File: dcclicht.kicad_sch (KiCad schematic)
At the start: 46 parts, among them J101 Power IN, J102 Debug, J103 CAN, Q101 BC860, SW101 Term, SW102 Reset, SW103 User, U101 AMS1117-3.3, U102 EL817S1(C)(TU)-F, U103 EL817S1(C)(TU)-F, U104 STM32F103CBTx, U105 TJA1042T, U106 ATECC608B-MAVDA-S, Y101 8MHz, Y102 32k

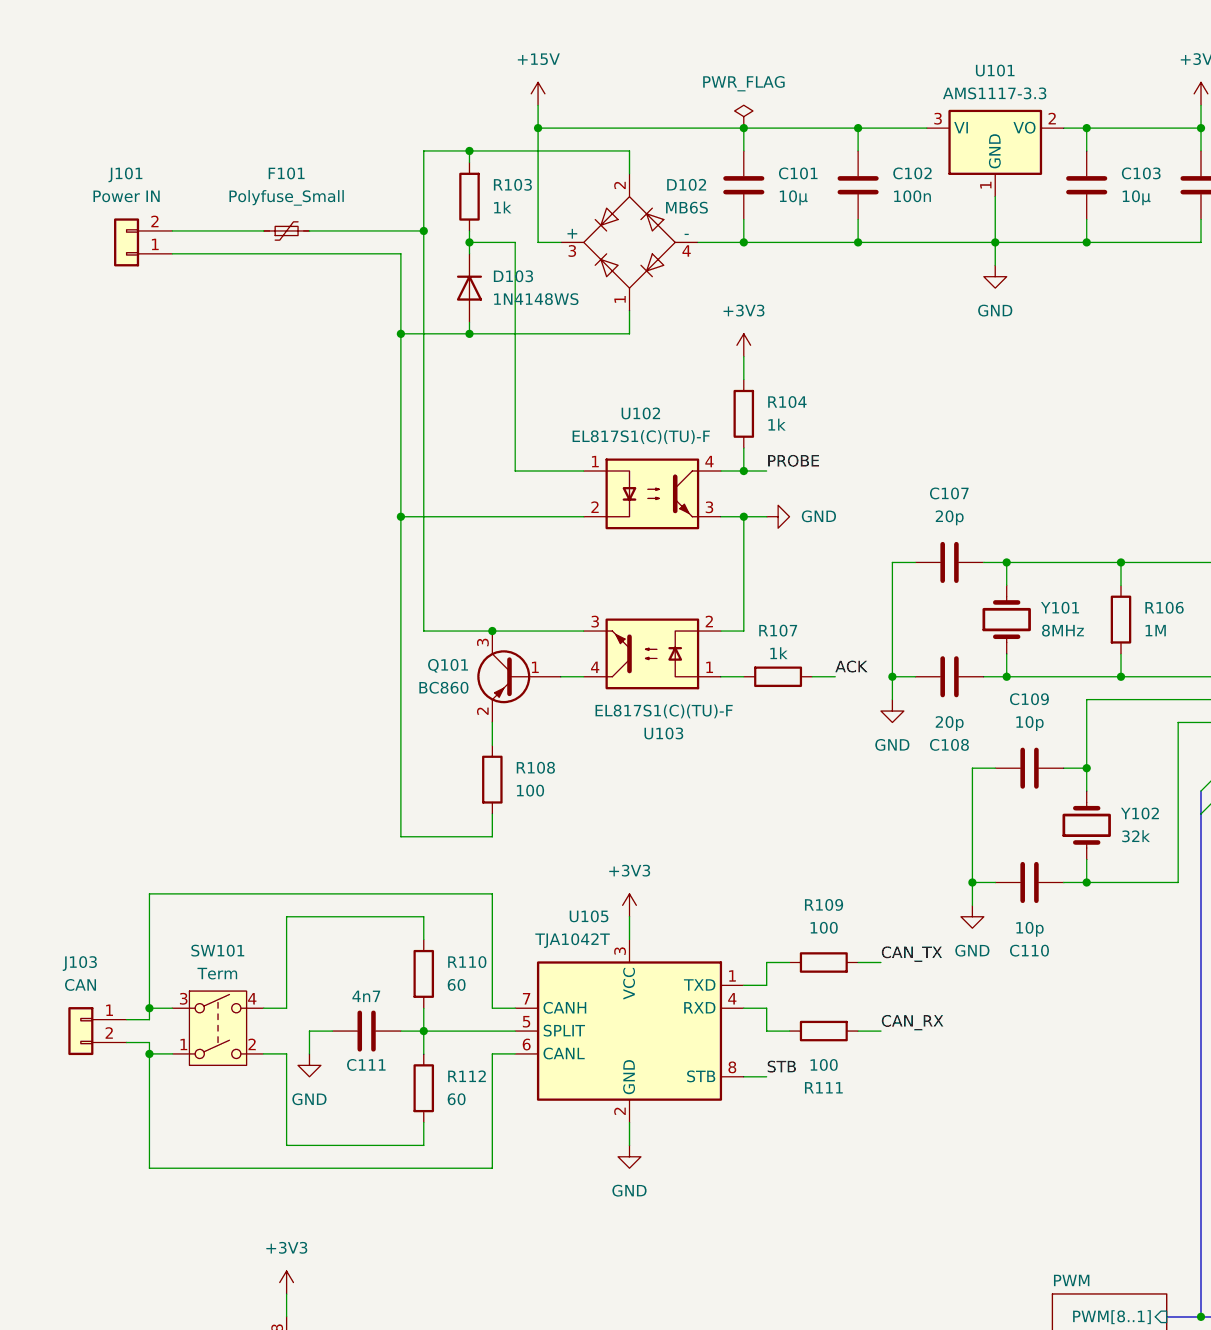
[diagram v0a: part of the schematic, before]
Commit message: Rework parts and order informations
Signed-off-by: Benedikt Spranger <b.spranger@linutronix.de>
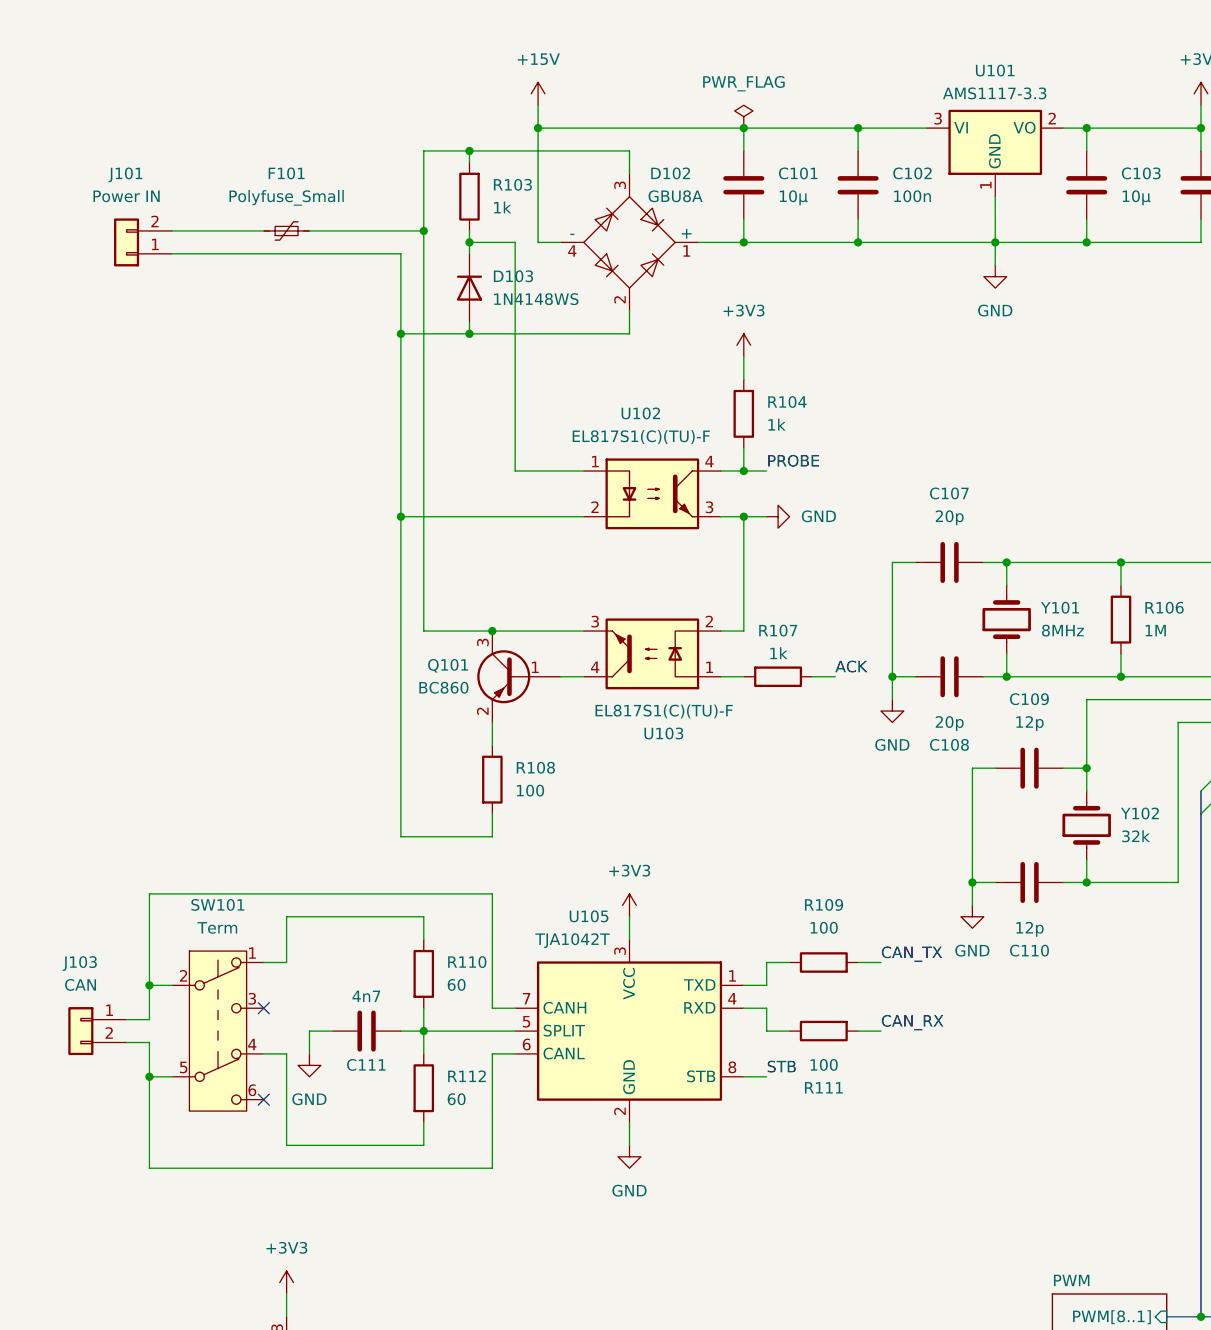
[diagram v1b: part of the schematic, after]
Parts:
- removed D102: MB6S, Package_TO_SOT_SMD:TO-269AA, symbol Diode_Bridge:MB6S
- removed SW101: Term, symbol Switch:SW_DPST
- added D102: GBU8A, Diode_THT:Diode_Bridge_Vishay_GBU, symbol Diode_Bridge:GBU8A
- added SW101: Term, Button_Switch_THT:SW_Push_2P2T_Toggle_CK_PVA2xxH1xxxxxxV2, symbol Switch:SW_Push_DPDT
- C101, C103: footprint (none) -> Capacitor_SMD:C_1206_3216Metric; LCSC# (none) -> C13585; Manufacture (none) -> Samsung Electro-Mechanics; assemble (none) -> y; mpn (none) -> CL31A106KBHNNNE
- C102, C104, C105, C112, C113: footprint (none) -> Capacitor_SMD:C_0402_1005Metric; LCSC# (none) -> C307331; Manufacture (none) -> Samsung Electro-Mechanics; assemble (none) -> y; mpn (none) -> CL05B104KB54PNC
- C106: footprint (none) -> Capacitor_THT:CP_Radial_D8.0mm_P3.50mm; Manufacture (none) -> SPSCAP; TME# (none) -> SCV1F-3.0V-LTZ; assemble (none) -> n; mpn (none) -> SCV0001C0-003R0LTZ
- C107, C108: footprint (none) -> Capacitor_SMD:C_0402_1005Metric; LCSC# (none) -> C1554; Manufacture (none) -> FH (Guangdong Fenghua Advanced Tech); assemble (none) -> y; mpn (none) -> 0402CG200J500NT
- C109, C110: value 10p -> 12p; footprint (none) -> Capacitor_SMD:C_0402_1005Metric; LCSC# (none) -> C1547; Manufacture (none) -> FH (Guangdong Fenghua Advanced Tech); assemble (none) -> y; mpn (none) -> 0402CG120J500NT
- C111: footprint (none) -> Capacitor_SMD:C_0402_1005Metric; LCSC# (none) -> C1538; Manufacture (none) -> FH (Guangdong Fenghua Advanced Tech); assemble (none) -> y; mpn (none) -> 0402B472K500NT
- D101: footprint (none) -> LED_SMD:LED_0603_1608Metric; LCSC# (none) -> C2286; Manufacture (none) -> Hubei KENTO Elec; assemble (none) -> y; mpn (none) -> KT-0603R
- D103, D104: LCSC# (none) -> C2128; Manufacture (none) -> Jiangsu Changjing Electronics Technology Co., Ltd.; assemble (none) -> y; mpn (none) -> 1N4148WS
- F101: footprint (none) -> Fuse:Fuse_2920_7451Metric; LCSC# (none) -> C495350; Manufacture (none) -> PTTC(Polytronics Tech); assemble (none) -> y; mpn (none) -> SHV2920P500-30-AA
- J101: footprint (none) -> TerminalBlock_WAGO:TerminalBlock_WAGO_233-502_2x02_P2.54mm; Digikey# (none) -> 2946-233-502-ND; Manufacture (none) -> WAGO Corporation; assemble (none) -> n; mpn (none) -> 233-502
- J102: Manufacture (none) -> N/A; assemble (none) -> n; mpn (none) -> N/A
- J103: footprint (none) -> TerminalBlock_WAGO:TerminalBlock_WAGO_236-402_1x02_P5.00mm_45Degree; Digikey# (none) -> 2946-236-402-ND; Manufacture (none) -> WAGO Corporation; assemble (none) -> n; mpn (none) -> 236-402
- JP101: footprint (none) -> Jumper:SolderJumper-2_P1.3mm_Open_Pad1.0x1.5mm; Manufacture (none) -> N/A; assemble (none) -> n; mpn (none) -> N/A
- Q101: LCSC# (none) -> C475637; Manufacture (none) -> Shikues; assemble (none) -> y; mpn (none) -> BC860B
- R101, R103, R104, R107: footprint (none) -> Resistor_SMD:R_0402_1005Metric; LCSC# (none) -> C11702; Manufacture (none) -> UNI-ROYAL(Uniroyal Elec); assemble (none) -> y; mpn (none) -> 0402WGF1001TCE
- R102: footprint (none) -> Resistor_SMD:R_0402_1005Metric; LCSC# (none) -> C25744; Manufacture (none) -> UNI-ROYAL(Uniroyal Elec); assemble (none) -> y; mpn (none) -> 0402WGF1002TCE
- R105: footprint (none) -> Resistor_SMD:R_0402_1005Metric; LCSC# (none) -> C25092; Manufacture (none) -> UNI-ROYAL(Uniroyal Elec); assemble (none) -> y; mpn (none) -> 0402WGF220JTCE
- R106: footprint (none) -> Resistor_SMD:R_0402_1005Metric; LCSC# (none) -> C26083; Manufacture (none) -> UNI-ROYAL(Uniroyal Elec); assemble (none) -> y; mpn (none) -> 0402WGF1004TCE
- R108: Manufacture (none) -> ROYALOHM; TME# (none) -> 3W-100R; assemble (none) -> n; mpn (none) -> MOR03SJ0101A19
- R109, R111: footprint (none) -> Resistor_SMD:R_0402_1005Metric; LCSC# (none) -> C25076; Manufacture (none) -> UNI-ROYAL(Uniroyal Elec); assemble (none) -> y; mpn (none) -> 0402WGF1000TCE
- R110, R112: footprint (none) -> Resistor_SMD:R_1206_3216Metric; LCSC# (none) -> C57572; Manufacture (none) -> UNI-ROYAL(Uniroyal Elec); assemble (none) -> y; mpn (none) -> 1206W4F604JT5E
- SW102, SW103: footprint (none) -> Button_Switch_THT:SW_PUSH_6mm; Manufacture (none) -> NINIGI; TME# (none) -> TACT-65R-F; assemble (none) -> n; mpn (none) -> TACT-65R-F
- U101: LCSC# (none) -> C6186; Manufacture (none) -> Advanced Monolithic Systems; assemble (none) -> y; mpn (none) -> AMS1117-3.3
- U102, U103: LCSC# (none) -> C106900; Manufacture (none) -> Everlight Elec; assemble (none) -> y; mpn (none) -> EL817S1(C)(TU)-F
- U104: LCSC# (none) -> C8304; Manufacture (none) -> STMicroelectronics; assemble (none) -> y; mpn (none) -> STM32F103CBT6
- U105: LCSC# (none) -> C53670; Manufacture (none) -> NXP Semicon; assemble (none) -> y; mpn (none) -> TJA1042T/1J
- U106: LCSC# (none) -> C17350254; Manufacture (none) -> Microchip Tech; assemble (none) -> y; mpn (none) -> ATECC608B-MAVDA-S
- Y101: footprint (none) -> Crystal:Crystal_SMD_HC49-SD; LCSC# (none) -> C12674; Manufacture (none) -> YXC Crystal Oscillators; assemble (none) -> y; mpn (none) -> X49SM8MSD2SC
- Y102: footprint (none) -> Crystal:Crystal_SMD_3215-2Pin_3.2x1.5mm; LCSC# (none) -> C32346; Manufacture (none) -> Seiko Epson; assemble (none) -> y; mpn (none) -> Q13FC13500004
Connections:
- net +15V: now also D102.4 (-)
- net GND: now also D102.1 (+)
- net at F101.2, Q101.3 (C), R103.2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: now also D102.3
- net at D103.2 (A), J101.1 (Pin_1), R108.2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: now also D102.2
- net at J103.2 (Pin_2), U105.6 (CANL): now also SW101.5 (B)
- net at J103.1 (Pin_1), U105.7 (CANH): now also SW101.2 (B)
- net at R112.2: now also SW101.4 (A)
- net at R110.1: now also SW101.1 (A)
- no-connect marks 12 -> 14

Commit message: Initial layout
Signed-off-by: Benedikt Spranger <b.spranger@linutronix.de>
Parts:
- added C101, C102, C103, C104: 100n, Capacitor_SMD:C_0402_1005Metric, symbol Device:C
- added H101, H102, H103, H104: ~, MountingHole:MountingHole_3.2mm_M3_ISO14580_Pad, symbol Mechanical:MountingHole_Pad
- J101: footprint TerminalBlock_WAGO:TerminalBlock_WAGO_233-502_2x02_P2.54mm -> TerminalBlock_WAGO:TerminalBlock_WAGO_236-402_1x02_P5.00mm_45Degree; Digikey# 2946-233-502-ND -> 2946-236-402/334-604-ND; mpn 233-502 -> 236-402/334-604
- renumbered C101 to C105, C102 to C106, C103 to C107, C104 to C108, C105 to C109, C106 to C110, C107 to C111, C108 to C112, C109 to C113, C110 to C114, C111 to C115, C112 to C116, C113 to C117
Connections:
- net +3V3: now also C101.1, C102.1, C103.1, C104.1
- net GND: now also C101.2, C102.2, C103.2, C104.2, H101.1, H102.1, H103.1, H104.1
- net PWM1: now also U104.19 (PB1); no longer U104.10 (PA0)
- net PWM2: now also U104.18 (PB0); no longer U104.11 (PA1)
- net PWM3: now also U104.17 (PA7); no longer U104.12 (PA2)
- net PWM4: now also U104.16 (PA6); no longer U104.13 (PA3)
- net PWM5: now also U104.13 (PA3); no longer U104.16 (PA6)
- net PWM6: now also U104.12 (PA2); no longer U104.17 (PA7)
- net PWM7: now also U104.11 (PA1); no longer U104.18 (PB0)
- net PWM8: now also U104.10 (PA0); no longer U104.19 (PB1)
- net at J103.2 (Pin_2), SW101.5 (B): now also U105.7 (CANH); no longer U105.6 (CANL)
- net at J103.1 (Pin_1), SW101.2 (B): now also U105.6 (CANL); no longer U105.7 (CANH)
- net at SW101.1 (A): no longer R110.1
- net at SW101.3 (C): now also R112.2
- net at SW101.4 (A): no longer R112.2
- net at SW101.6 (C): now also R110.1
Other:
- moved on the sheet: J103, JP101, R102

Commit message: Add legalese
Signed-off-by: Benedikt Spranger <b.spranger@linutronix.de>
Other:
- company: (none) -> Eurovibes Benedikt Spranger
- title: (none) -> DCC Licht
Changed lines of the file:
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@@
 	(paper "A4")
 	(title_block
+		(title "DCC Licht")
 		(date "2025-01-22")
 		(rev "v0.1")
+		(company "Eurovibes Benedikt Spranger")
+		(comment 1 "SPDX-License-Identifier: CERN-OHL-S-2.0")
+		(comment 2 "https://ohwr.org/cern_ohl_s_v2.txt")
+		(comment 3 "To view a copy of this license, visit")
+		(comment 4 "This work is licensed under the CERN-OHL-S v2")
 	)
 	(junction

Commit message: Add alternate source for TL2202EEYB
Signed-off-by: Benedikt Spranger <b.spranger@linutronix.de>
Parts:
- SW101: TME# (none) -> TL2202EEYB
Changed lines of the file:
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@@
+			)
+		)
+		(property "TME#" "TL2202EEYB"
+			(at 43.18 133.35 0)
+			(effects
+				(font
+					(size 1.27 1.27)
+				)
+				(hide yes)
 			)
 		)

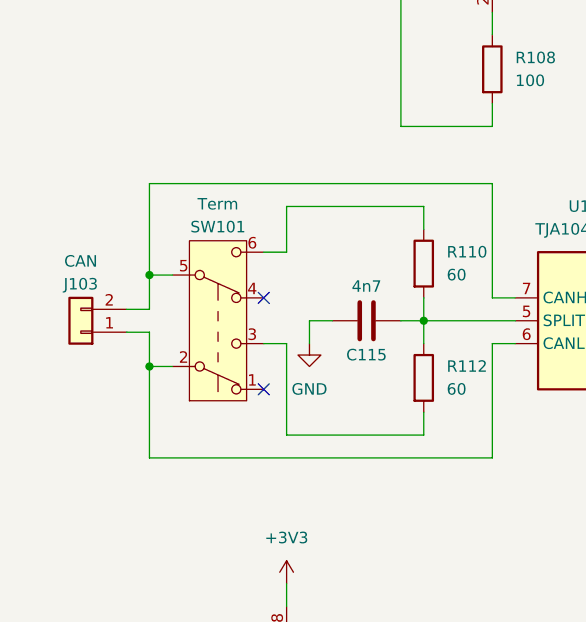
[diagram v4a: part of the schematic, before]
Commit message: Add signal names foe CAN high/low
Signed-off-by: Benedikt Spranger <b.spranger@linutronix.de>
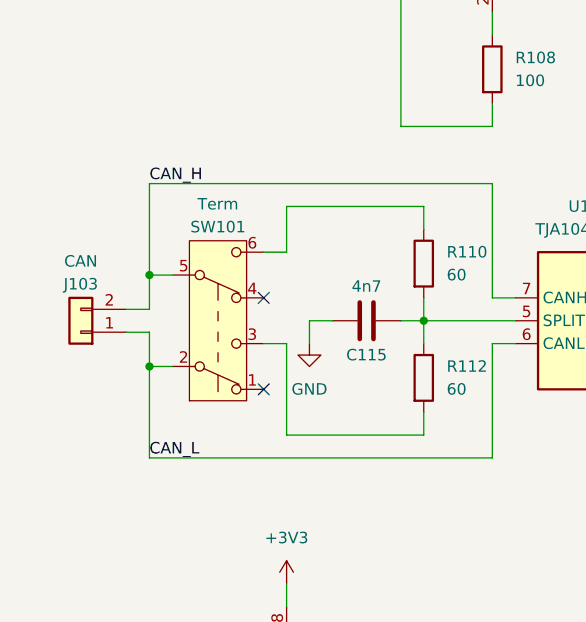
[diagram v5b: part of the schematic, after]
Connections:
- net CAN_L: now reaches J103.1 (Pin_1), SW101.2 (B), U105.6 (CANL)
- net CAN_H: now reaches J103.2 (Pin_2), SW101.5 (B), U105.7 (CANH)
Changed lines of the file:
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@@
+		)
+	)
+	(label "CAN_H"
+		(at 35.56 118.11 0)
+		(effects
+			(font
+				(size 1.27 1.27)
+			)
+			(justify left bottom)
 		)
 	)
@@
 		(effects
 			(font
+				(size 1.27 1.27)
+			)
+			(justify left bottom)
+		)
+	)
+	(label "CAN_L"
+		(at 35.56 148.59 0)
+		(effects
+			(font

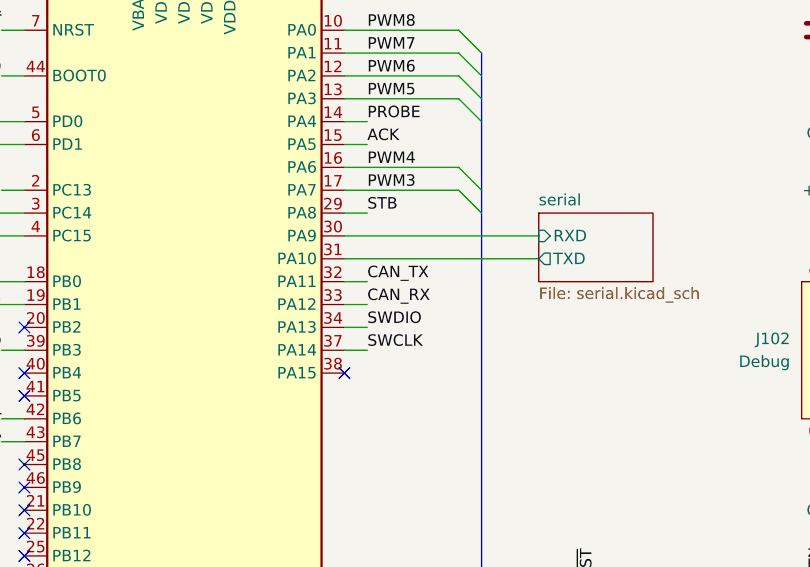
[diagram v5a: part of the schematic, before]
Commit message: Switch CAN_RX and CAN_TX signals
Signed-off-by: Benedikt Spranger <b.spranger@linutronix.de>
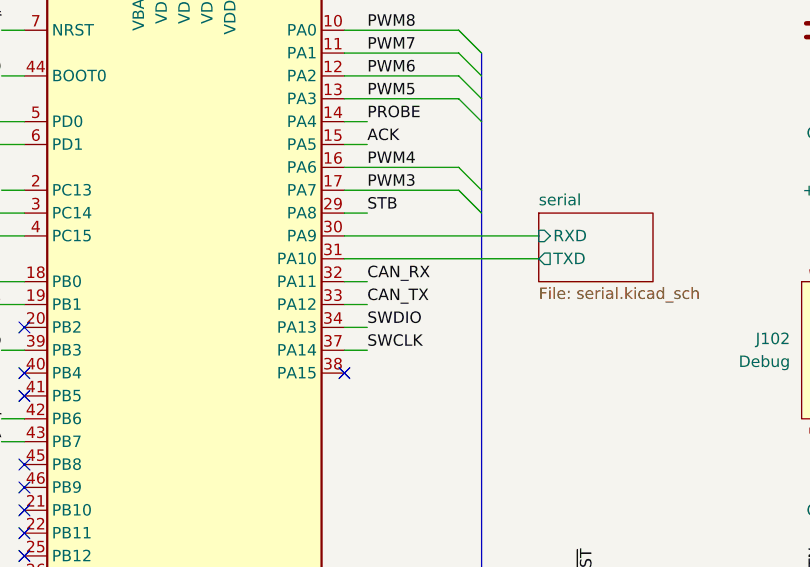
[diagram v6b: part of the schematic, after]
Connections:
- net CAN_RX: now also U104.32 (PA11); no longer U104.33 (PA12)
- net CAN_TX: now also U104.33 (PA12); no longer U104.32 (PA11)
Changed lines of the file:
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@@
 	)
 	(label "CAN_RX"
-		(at 203.2 106.68 0)
+		(at 203.2 104.14 0)
 		(effects
 			(font
@@
 	)
 	(label "CAN_TX"
-		(at 203.2 104.14 0)
+		(at 203.2 106.68 0)
 		(effects
 			(font
